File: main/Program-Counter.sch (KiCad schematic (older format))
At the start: 6 parts, among them U89 74LS161, U90 74LS245, U91 74LS161, U92 74LS245, U93 74LS161, U94 74LS161

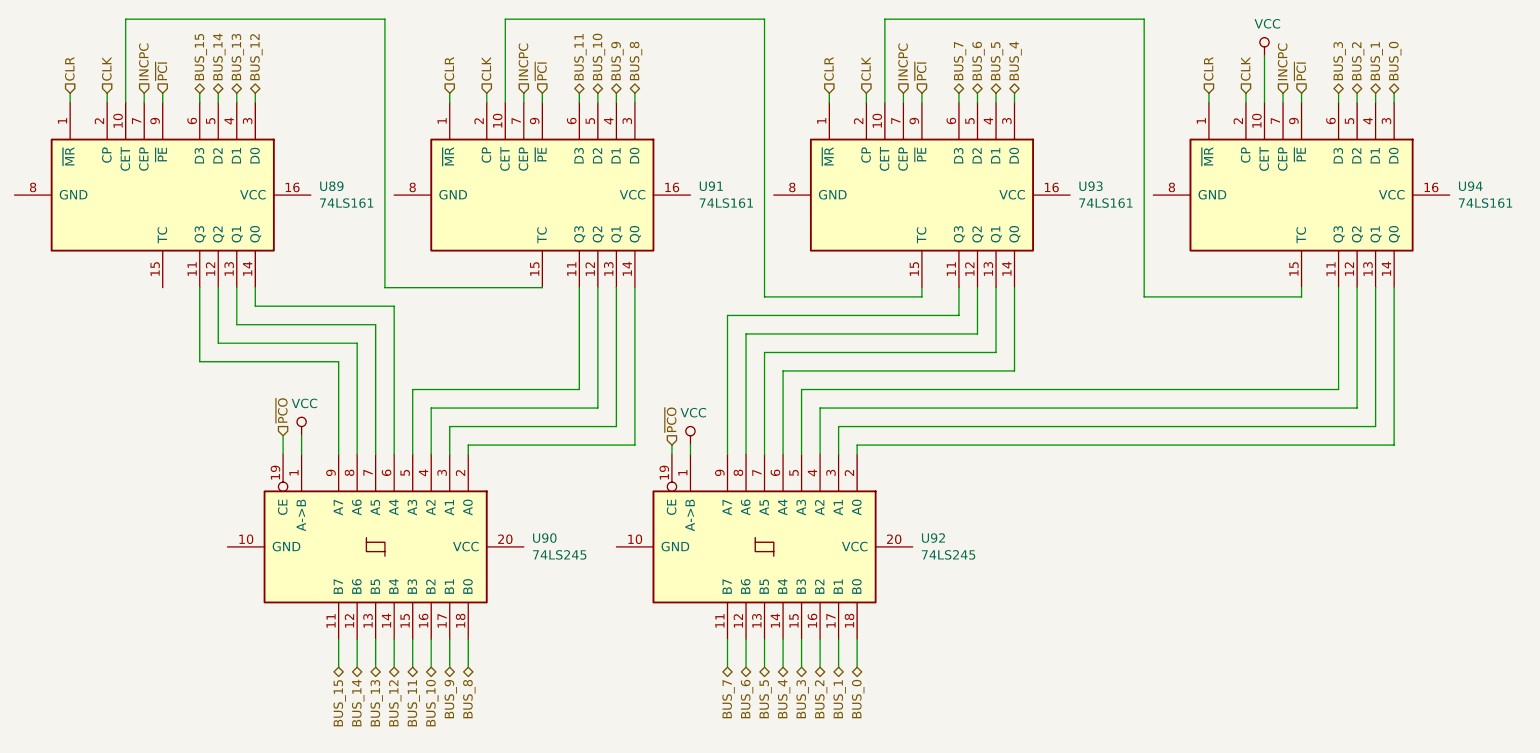
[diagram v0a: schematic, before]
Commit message: Replot main with symbols
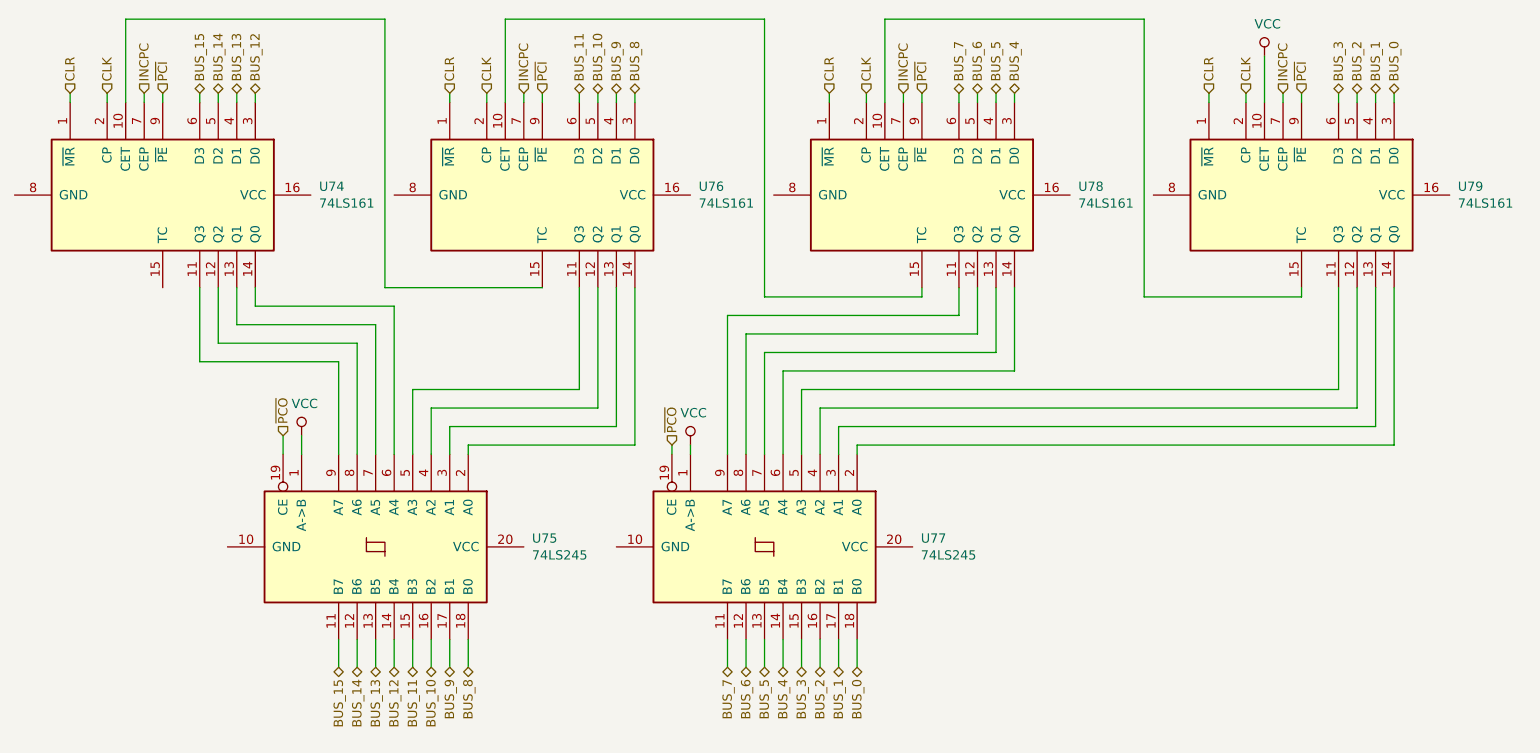
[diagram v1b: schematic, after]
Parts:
- renumbered U89 to U74, U90 to U75, U91 to U76, U92 to U77, U93 to U78, U94 to U79
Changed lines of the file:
@@
 Sheet 21 26
 Title "Program Counter"
-Date "2019-11-13"
+Date "2019-11-17"
 Rev "v1.0"
 Comp "Christopher Milan"
@@
 ~PCI~
 $Comp
-L 74xx:74LS161 U89
+L 74xx:74LS161 U74
 U 1 1 605241F8
 P 2550 3000
-F 0 "U89" V 2504 3844 50  0000 L CNN
+F 0 "U74" V 2504 3844 50  0000 L CNN
 F 1 "74LS161" V 2595 3844 50  0000 L CNN
 F 2 "" H 2550 3000 50  0001 C CNN
@@
 $EndComp
 $Comp
-L 74xx:74LS161 U91
+L 74xx:74LS161 U76
 U 1 1 60528F0E
 P 4600 3000
-F 0 "U91" V 4554 3844 50  0000 L CNN
+F 0 "U76" V 4554 3844 50  0000 L CNN
 F 1 "74LS161" V 4645 3844 50  0000 L CNN
 F 2 "" H 4600 3000 50  0001 C CNN
@@
 $EndComp
 $Comp
-L 74xx:74LS161 U93
+L 74xx:74LS161 U78
 U 1 1 6052CF75
 P 6650 3000
-F 0 "U93" V 6604 3844 50  0000 L CNN
+F 0 "U78" V 6604 3844 50  0000 L CNN
 F 1 "74LS161" V 6695 3844 50  0000 L CNN
 F 2 "" H 6650 3000 50  0001 C CNN
@@
 $EndComp
 $Comp
-L 74xx:74LS161 U94
+L 74xx:74LS161 U79
 U 1 1 6052CF7B
 P 8700 3000
-F 0 "U94" V 8654 3844 50  0000 L CNN
+F 0 "U79" V 8654 3844 50  0000 L CNN
 F 1 "74LS161" V 8745 3844 50  0000 L CNN
 F 2 "" H 8700 3000 50  0001 C CNN
@@
 	2350 2050 2350 2500
 $Comp
-L 74xx:74LS245 U90
+L 74xx:74LS245 U75
 U 1 1 60546328
 P 3700 4900
-F 0 "U90" V 3654 5744 50  0000 L CNN
+F 0 "U75" V 3654 5744 50  0000 L CNN
 F 1 "74LS245" V 3745 5744 50  0000 L CNN
 F 2 "" H 3700 4900 50  0001 C CNN
@@
 $EndComp
 $Comp
-L 74xx:74LS245 U92
+L 74xx:74LS245 U77
 U 1 1 6054B8F9
 P 5800 4900
-F 0 "U92" V 5754 5744 50  0000 L CNN
+F 0 "U77" V 5754 5744 50  0000 L CNN
 F 1 "74LS245" V 5845 5744 50  0000 L CNN
 F 2 "" H 5800 4900 50  0001 C CNN
